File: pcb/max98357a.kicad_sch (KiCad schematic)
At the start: 6 parts, among them J4 MAX98357A Breakout

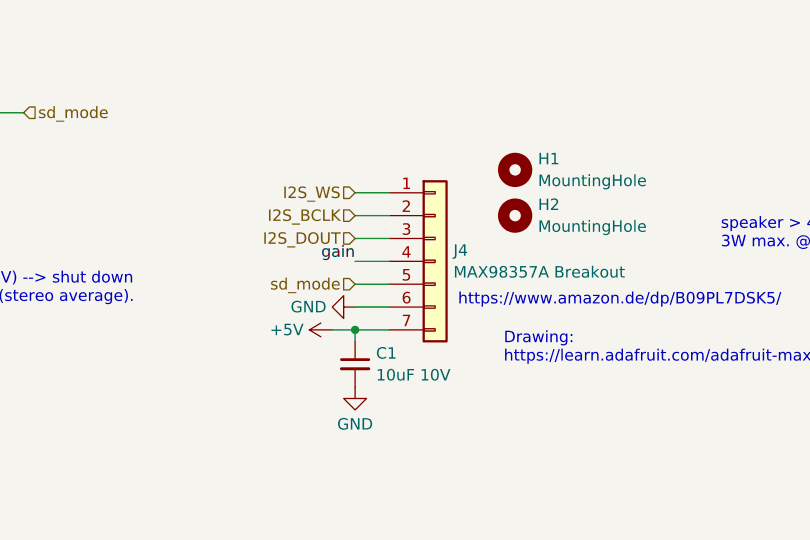
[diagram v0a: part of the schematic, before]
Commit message: work on PCB: line out + power done ; removed amplifier from board
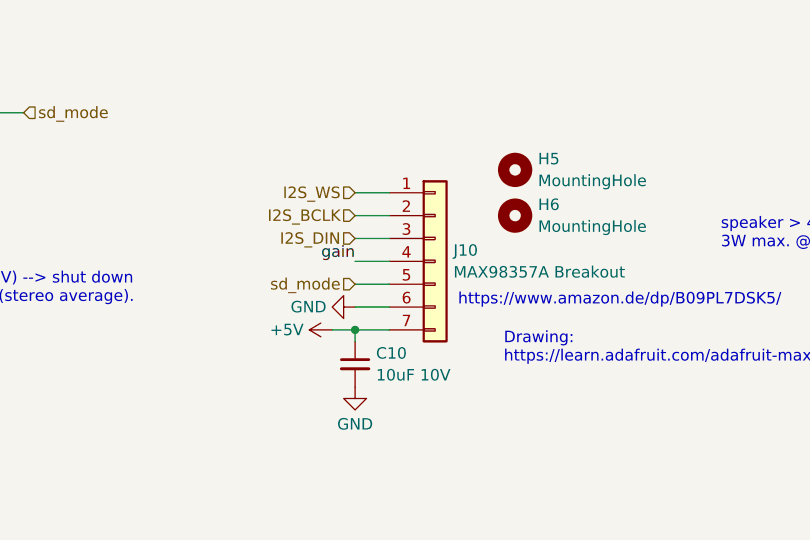
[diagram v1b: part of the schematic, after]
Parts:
- renumbered C1 to C10, H1 to H5, H2 to H6, J4 to J10
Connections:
- net I2S_DOUT renamed I2S_DIN
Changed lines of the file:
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@@
     (effects (font (size 1.27 1.27)) (justify left))
   )
-  (hierarchical_label "I2S_DOUT" (shape input) (at 149.86 88.9 180) (fields_autoplaced)
+  (hierarchical_label "I2S_DIN" (shape input) (at 149.86 88.9 180) (fields_autoplaced)
     (effects (font (size 1.27 1.27)) (justify right))
   )
@@
   )
   (symbol (lib_id "Jumper:SolderJumper_3_Open") (at 78.74 114.3 90) (unit 1)
-    (in_bom yes) (on_board yes) (dnp no) (fields_autoplaced)
+    (in_bom yes) (on_board no) (dnp no) (fields_autoplaced)
     (property "Reference" "JP2" (at 77.089 113.0879 90)
       (effects (font (size 1.27 1.27)) (justify left))
@@
   (symbol (lib_id "power:GND") (at 78.74 80.01 0) (unit 1)
     (in_bom yes) (on_board yes) (dnp no) (fields_autoplaced)
-    (property "Reference" "#PWR05" (at 78.74 86.36 0)
+    (property "Reference" "#PWR042" (at 78.74 86.36 0)
       (effects (font (size 1.27 1.27)) hide)
     )
@@
       (project "wakeuplight"
         (path "/f5441fcc-7db8-443c-8d47-1d2e67dbd624/297f229e-b770-41aa-886e-ef043aa938c5"
-          (reference "#PWR05") (unit 1)
+          (reference "#PWR042") (unit 1)
         )
       )
@@
   )
   (symbol (lib_id "Mechanical:MountingHole") (at 167.64 81.28 0) (unit 1)
-    (in_bom yes) (on_board yes) (dnp no) (fields_autoplaced)
-    (property "Reference" "H1" (at 170.18 80.0679 0)
+    (in_bom yes) (on_board no) (dnp no) (fields_autoplaced)
+    (property "Reference" "H5" (at 170.18 80.0679 0)
       (effects (font (size 1.27 1.27)) (justify left))
     )
@@
       (project "wakeuplight"
         (path "/f5441fcc-7db8-443c-8d47-1d2e67dbd624/297f229e-b770-41aa-886e-ef043aa938c5"
-          (reference "H1") (unit 1)
+          (reference "H5") (unit 1)
         )
       )
@@
   (symbol (lib_id "power:GND") (at 149.86 105.41 0) (unit 1)
     (in_bom yes) (on_board yes) (dnp no) (fields_autoplaced)
-    (property "Reference" "#PWR041" (at 149.86 111.76 0)
+    (property "Reference" "#PWR047" (at 149.86 111.76 0)
       (effects (font (size 1.27 1.27)) hide)
     )
@@
       (project "wakeuplight"
         (path "/f5441fcc-7db8-443c-8d47-1d2e67dbd624/297f229e-b770-41aa-886e-ef043aa938c5"
-          (reference "#PWR041") (unit 1)
+          (reference "#PWR047") (unit 1)
         )
       )
@@
   )
   (symbol (lib_id "Connector_Generic:Conn_01x07") (at 158.75 91.44 0) (unit 1)
-    (in_bom yes) (on_board yes) (dnp no) (fields_autoplaced)
-    (property "Reference" "J4" (at 160.782 90.2279 0)
+    (in_bom yes) (on_board no) (dnp no) (fields_autoplaced)
+    (property "Reference" "J10" (at 160.782 90.2279 0)
       (effects (font (size 1.27 1.27)) (justify left))
     )
@@
       (project "wakeuplight"
         (path "/f5441fcc-7db8-443c-8d47-1d2e67dbd624/297f229e-b770-41aa-886e-ef043aa938c5"
-          (reference "J4") (unit 1)
+          (reference "J10") (unit 1)
         )
       )
@@
   )
   (symbol (lib_id "Device:C_Small") (at 149.86 102.87 0) (unit 1)
-    (in_bom yes) (on_board yes) (dnp no) (fields_autoplaced)
-    (property "Reference" "C1" (at 152.1841 101.6642 0)
+    (in_bom yes) (on_board no) (dnp no) (fields_autoplaced)
+    (property "Reference" "C10" (at 152.1841 101.6642 0)
       (effects (font (size 1.27 1.27)) (justify left))
     )
@@
       (project "wakeuplight"
         (path "/f5441fcc-7db8-443c-8d47-1d2e67dbd624/297f229e-b770-41aa-886e-ef043aa938c5"
-          (reference "C1") (unit 1)
+          (reference "C10") (unit 1)
         )
       )
@@
   (symbol (lib_id "power:GND") (at 78.74 119.38 0) (unit 1)
     (in_bom yes) (on_board yes) (dnp no) (fields_autoplaced)
-    (property "Reference" "#PWR011" (at 78.74 125.73 0)
+    (property "Reference" "#PWR044" (at 78.74 125.73 0)
       (effects (font (size 1.27 1.27)) hide)
     )
@@
       (project "wakeuplight"
         (path "/f5441fcc-7db8-443c-8d47-1d2e67dbd624/297f229e-b770-41aa-886e-ef043aa938c5"
-          (reference "#PWR011") (unit 1)
+          (reference "#PWR044") (unit 1)
         )
       )
@@
   (symbol (lib_id "power:+5V") (at 147.32 99.06 90) (unit 1)
     (in_bom yes) (on_board yes) (dnp no) (fields_autoplaced)
-    (property "Reference" "#PWR039" (at 151.13 99.06 0)
+    (property "Reference" "#PWR045" (at 151.13 99.06 0)
       (effects (font (size 1.27 1.27)) hide)
     )
@@
       (project "wakeuplight"
         (path "/f5441fcc-7db8-443c-8d47-1d2e67dbd624/297f229e-b770-41aa-886e-ef043aa938c5"
-          (reference "#PWR039") (unit 1)
+          (reference "#PWR045") (unit 1)
         )
       )
@@
   )
   (symbol (lib_id "Jumper:SolderJumper_3_Open") (at 78.74 74.93 90) (unit 1)
-    (in_bom yes) (on_board yes) (dnp no) (fields_autoplaced)
+    (in_bom yes) (on_board no) (dnp no) (fields_autoplaced)
     (property "Reference" "JP1" (at 77.089 73.7179 90)
       (effects (font (size 1.27 1.27)) (justify left))
@@
   )
   (symbol (lib_id "Mechanical:MountingHole") (at 167.64 86.36 0) (unit 1)
-    (in_bom yes) (on_board yes) (dnp no) (fields_autoplaced)
-    (property "Reference" "H2" (at 170.18 85.1479 0)
+    (in_bom yes) (on_board no) (dnp no) (fields_autoplaced)
+    (property "Reference" "H6" (at 170.18 85.1479 0)
       (effects (font (size 1.27 1.27)) (justify left))
     )
@@
       (project "wakeuplight"
         (path "/f5441fcc-7db8-443c-8d47-1d2e67dbd624/297f229e-b770-41aa-886e-ef043aa938c5"
-          (reference "H2") (unit 1)
+          (reference "H6") (unit 1)
         )
       )
@@
   (symbol (lib_id "power:+5V") (at 78.74 109.22 0) (unit 1)
     (in_bom yes) (on_board yes) (dnp no) (fields_autoplaced)
-    (property "Reference" "#PWR010" (at 78.74 113.03 0)
+    (property "Reference" "#PWR043" (at 78.74 113.03 0)
       (effects (font (size 1.27 1.27)) hide)
     )
@@
       (project "wakeuplight"
         (path "/f5441fcc-7db8-443c-8d47-1d2e67dbd624/297f229e-b770-41aa-886e-ef043aa938c5"
-          (reference "#PWR010") (unit 1)
+          (reference "#PWR043") (unit 1)
         )
       )
@@
   (symbol (lib_id "power:+5V") (at 78.74 69.85 0) (unit 1)
     (in_bom yes) (on_board yes) (dnp no) (fields_autoplaced)
-    (property "Reference" "#PWR04" (at 78.74 73.66 0)
+    (property "Reference" "#PWR041" (at 78.74 73.66 0)
       (effects (font (size 1.27 1.27)) hide)
     )
@@
       (project "wakeuplight"
         (path "/f5441fcc-7db8-443c-8d47-1d2e67dbd624/297f229e-b770-41aa-886e-ef043aa938c5"
-          (reference "#PWR04") (unit 1)
+          (reference "#PWR041") (unit 1)
         )
       )
@@
   (symbol (lib_id "power:GND") (at 149.86 96.52 270) (unit 1)
     (in_bom yes) (on_board yes) (dnp no) (fields_autoplaced)
-    (property "Reference" "#PWR040" (at 143.51 96.52 0)
+    (property "Reference" "#PWR046" (at 143.51 96.52 0)
       (effects (font (size 1.27 1.27)) hide)
     )
@@
       (project "wakeuplight"
         (path "/f5441fcc-7db8-443c-8d47-1d2e67dbd624/297f229e-b770-41aa-886e-ef043aa938c5"
-          (reference "#PWR040") (unit 1)
-        )
-      )
+          (reference "#PWR046") (unit 1)
+        )
+      )
